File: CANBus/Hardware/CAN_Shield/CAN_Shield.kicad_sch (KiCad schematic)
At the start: 12 parts, among them J1 Power, J2 PWM, J3 Analog, J4 PWM, J5 Analog, J6 Communication, J7 Digital, J8 Screw_Terminal_01x02, U2 TCAN1051HGV

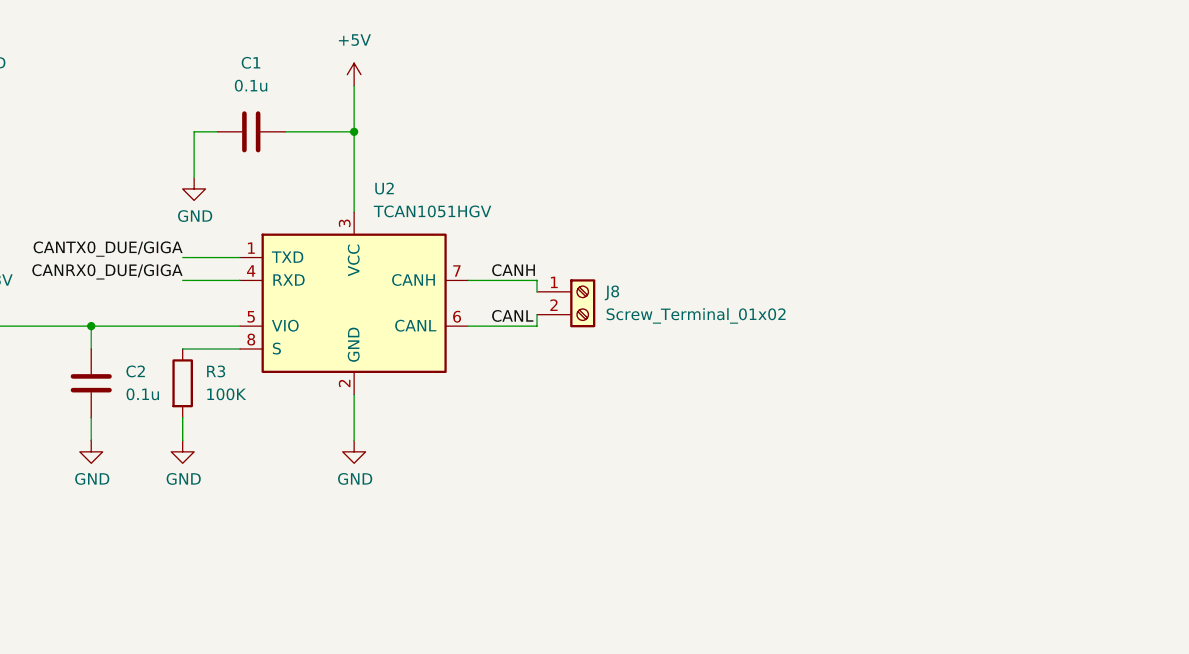
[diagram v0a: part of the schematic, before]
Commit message: feat: added  termination resistors and sent pin S to digital pin 2
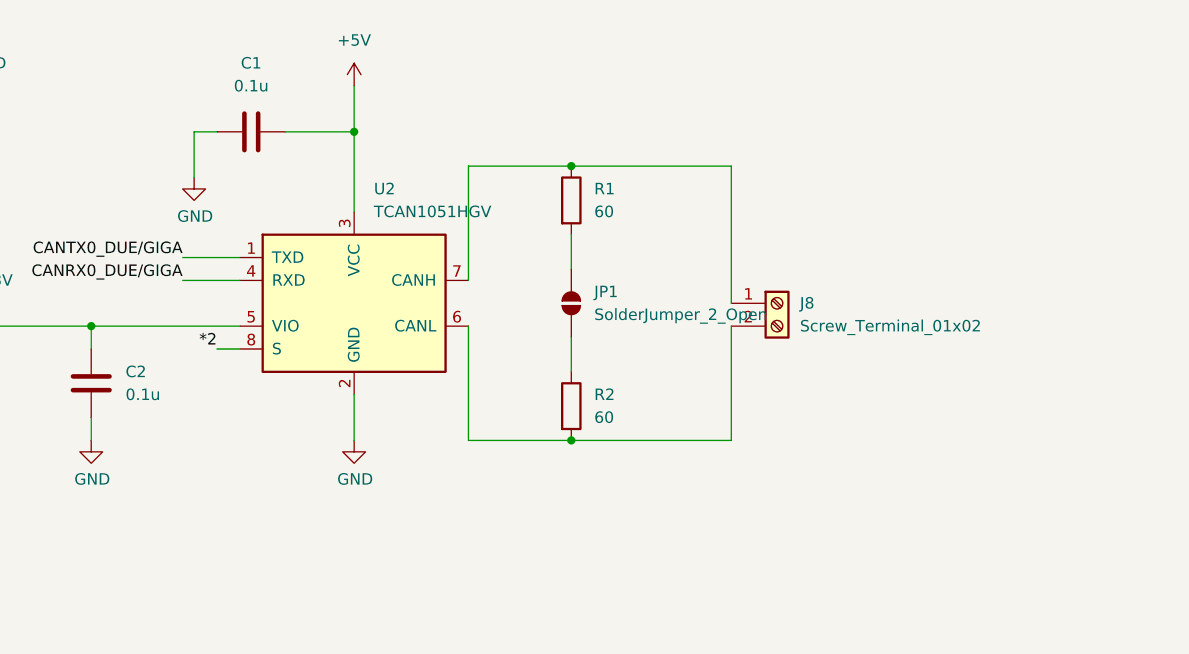
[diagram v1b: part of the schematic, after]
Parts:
- removed R3: 100K, symbol Device:R
- added JP1: SolderJumper_2_Open, symbol Jumper:SolderJumper_2_Open
- added R1, R2: 60, symbol Device:R
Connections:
- net *2: now also U2.8 (S)
- net CANH: no longer names the net of J8.1 (Pin_1), U2.7 (CANH)
- net CANH: now also R1.1
- net CANL: no longer names the net of J8.2 (Pin_2), U2.6 (CANL)
- net CANL: now also R2.2
- new net: JP1.1 (A), R2.1
- new net: JP1.2 (B), R1.2
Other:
- moved on the sheet: J8

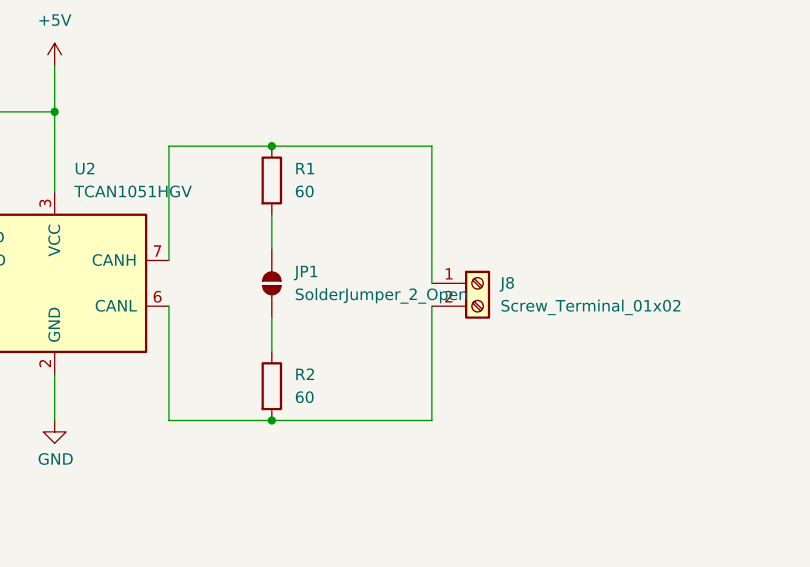
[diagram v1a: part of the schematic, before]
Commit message: fix: change to bridged solder jumper and remove backup files
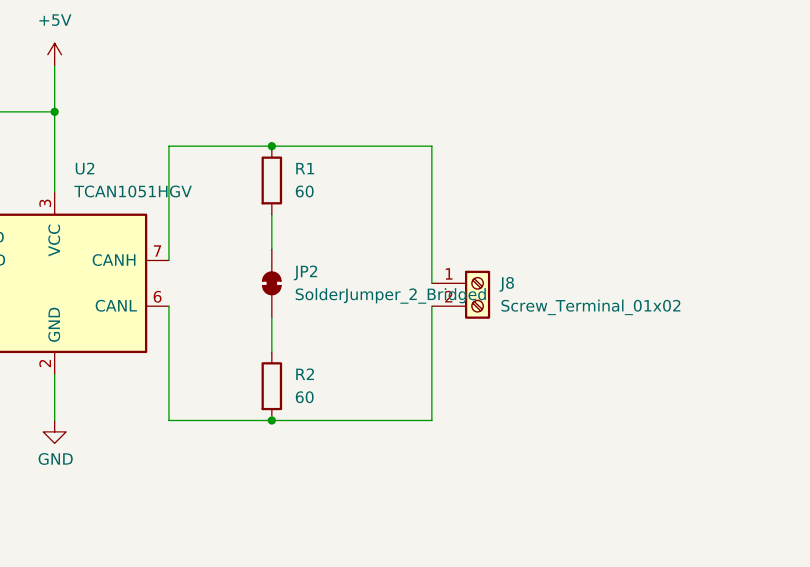
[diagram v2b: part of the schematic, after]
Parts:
- removed JP1: SolderJumper_2_Open, symbol Jumper:SolderJumper_2_Open
- added JP2: SolderJumper_2_Bridged, symbol Jumper:SolderJumper_2_Bridged
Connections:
- net at R2.1: now also JP2.1 (A)
- net at R1.2: now also JP2.2 (B)
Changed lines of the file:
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@@
 	(wire
 		(pts
-			(xy 146.05 71.12) (xy 146.05 74.93)
-		)
-		(stroke
-			(width 0)
-			(type default)
-		)
-	)
-	(wire
-		(pts
 			(xy 74.93 119.38) (xy 74.93 132.08)
 		)
@@
 	(wire
 		(pts
-			(xy 146.05 59.69) (xy 146.05 63.5)
-		)
-		(stroke
-			(width 0)
-			(type default)
-		)
-	)
-	(wire
-		(pts
 			(xy 20.32 46.99) (xy 20.32 49.53)
 		)
@@
 	(wire
 		(pts
+			(xy 146.05 71.12) (xy 146.05 74.93)
+		)
+		(stroke
+			(width 0)
+			(type default)
+		)
+	)
+	(wire
+		(pts
 			(xy 63.5 97.79) (xy 76.2 97.79)
 		)
@@
 	(wire
 		(pts
+			(xy 146.05 59.69) (xy 146.05 63.5)
+		)
+		(stroke
+			(width 0)
+			(type default)
+		)
+	)
+	(wire
+		(pts
 			(xy 39.37 132.08) (xy 39.37 142.24)
 		)
@@
 	)
 	(symbol
-		(lib_id "Jumper:SolderJumper_2_Open")
-		(at 146.05 67.31 90)
-		(unit 1)
-		(exclude_from_sim yes)
-		(in_bom no)
-		(on_board yes)
-		(dnp no)
-		(fields_autoplaced yes)
-		(property "Reference" "JP1"
-			(at 148.59 66.0399 90)
-			(effects
-				(font
-					(size 1.27 1.27)
-				)
-				(justify right)
-			)
-		)
-		(property "Value" "SolderJumper_2_Open"
-			(at 148.59 68.5799 90)
-			(effects
-				(font
-					(size 1.27 1.27)
-				)
-				(justify right)
-			)
-		)
-		(property "Footprint" ""
-			(at 146.05 67.31 0)
-			(effects
-				(font
-					(size 1.27 1.27)
-				)
-				(hide yes)
-			)
-		)
-		(property "Datasheet" "~"
-			(at 146.05 67.31 0)
-			(effects
-				(font
-					(size 1.27 1.27)
-				)
-				(hide yes)
-			)
-		)
-		(property "Description" "Solder Jumper, 2-pole, open"
-			(at 146.05 67.31 0)
-			(effects
-				(font
-					(size 1.27 1.27)
-				)
-				(hide yes)
-			)
-		)
-		(pin "1"
-		)
-		(pin "2"
-		)
-		(instances
-			(project "CAN_Shield"
-				(path "/e63e39d7-6ac0-4ffd-8aa3-1841a4541b55"
-					(reference "JP1")
-					(unit 1)
-				)
-			)
-		)
-	)
-	(symbol
 		(lib_id "power:VCC")
 		(at 26.67 26.67 0)
@@
 					(unit 1)
 				)
+			)
+		)
+	)
+	(symbol
+		(lib_id "Jumper:SolderJumper_2_Bridged")
+		(at 146.05 67.31 90)
+		(unit 1)
+		(exclude_from_sim yes)
+		(in_bom no)
+		(on_board yes)
+		(dnp no)
+		(fields_autoplaced yes)
+		(property "Reference" "JP2"
+			(at 148.59 66.0399 90)
+			(effects
+				(font
+					(size 1.27 1.27)
+				)
+				(justify right)
+			)
+		)
+		(property "Value" "SolderJumper_2_Bridged"
+			(at 148.59 68.5799 90)
+			(effects
+				(font
+					(size 1.27 1.27)
+				)
+				(justify right)
+			)
+		)
+		(property "Footprint" ""
+			(at 146.05 67.31 0)
+			(effects
+				(font
+					(size 1.27 1.27)
+				)
+				(hide yes)
+			)
+		)
+		(property "Datasheet" "~"
+			(at 146.05 67.31 0)
+			(effects
+				(font
+					(size 1.27 1.27)
+				)
+				(hide yes)
+			)
+		)
+		(property "Description" "Solder Jumper, 2-pole, closed/bridged"
+			(at 146.05 67.31 0)
+			(effects
+				(font
+					(size 1.27 1.27)
+				)
+				(hide yes)
+			)
+		)
+		(pin "2"
+		)
+		(pin "1"
+		)
+		(instances
+			(project "CAN_Shield"
+				(path "/e63e39d7-6ac0-4ffd-8aa3-1841a4541b55"
+					(reference "JP2")
+					(unit 1)
+				)

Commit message: feat: added PCB design
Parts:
- C1, C2: footprint (none) -> Capacitor_SMD:C_0805_2012Metric_Pad1.18x1.45mm_HandSolder; LCSC# (none) -> C38141; Proveedor (none) -> LCSC; manf# (none) -> 0805B104K500NT
- J1, J2, J3, J4, J5, J6: Proveedor (none) -> MOUSER/Digikey; manf# (none) -> PRT-14322
- J7: Proveedor (none) -> MOUSER; manf# (none) -> PRT-12790
- J8: footprint (none) -> TerminalBlock:TerminalBlock_bornier-2_P5.08mm; Proveedor (none) -> Steren; manf# (none) -> TRT-02
- JP2: footprint (none) -> Connector_PinHeader_2.54mm:PinHeader_1x02_P2.54mm_Vertical; LCSC# (none) -> C492401; Proveedor (none) -> LCSC; manf# (none) -> PZ254V-11-02P
- R1, R2: footprint (none) -> Resistor_SMD:R_0201_0603Metric; LCSC# (none) -> C166918; Proveedor (none) -> LCSC; manf# (none) -> RTT0360R0FTP
- U2: footprint (none) -> Package_SO:SOIC-8_3.9x4.9mm_P1.27mm; LCSC# (none) -> C424093; Proveedor (none) -> LCSC; manf# (none) -> MCP73831T-2ACI/OT
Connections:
- net +3.3V is gone; now on net +3V3: C2.1, U2.5 (VIO)

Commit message: feat: Resistors got changed
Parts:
- R1, R2: footprint Resistor_SMD:R_0201_0603Metric -> Resistor_SMD:R_1206_3216Metric_Pad1.30x1.75mm_HandSolder; LCSC# C166918 -> (none); Proveedor LCSC -> MOUSER; manf# RTT0360R0FTP -> 71-CRCW120660R0KNAIF
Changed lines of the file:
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@@
 			)
 		)
-		(property "Footprint" "Resistor_SMD:R_0201_0603Metric"
+		(property "Footprint" "Resistor_SMD:R_1206_3216Metric_Pad1.30x1.75mm_HandSolder"
 			(at 144.272 78.74 90)
 			(effects
@@
 			)
 		)
-		(property "LCSC#" " C166918"
-			(at 146.05 78.74 0)
-			(effects
-				(font
-					(size 1.27 1.27)
-				)
-				(hide yes)
-			)
-		)
-		(property "Proveedor" "LCSC"
-			(at 146.05 78.74 0)
-			(effects
-				(font
-					(size 1.27 1.27)
-				)
-				(hide yes)
-			)
-		)
-		(property "manf#" " RTT0360R0FTP"
+		(property "LCSC#" ""
+			(at 146.05 78.74 0)
+			(effects
+				(font
+					(size 1.27 1.27)
+				)
+				(hide yes)
+			)
+		)
+		(property "Proveedor" "MOUSER"
+			(at 146.05 78.74 0)
+			(effects
+				(font
+					(size 1.27 1.27)
+				)
+				(hide yes)
+			)
+		)
+		(property "manf#" "71-CRCW120660R0KNAIF"
 			(at 146.05 78.74 0)
 			(effects
@@
 			)
 		)
-		(property "Footprint" "Resistor_SMD:R_0201_0603Metric"
+		(property "Footprint" "Resistor_SMD:R_1206_3216Metric_Pad1.30x1.75mm_HandSolder"
 			(at 144.272 55.88 90)
 			(effects
@@
 			)
 		)
-		(property "LCSC#" " C166918"
-			(at 146.05 55.88 0)
-			(effects
-				(font
-					(size 1.27 1.27)
-				)
-				(hide yes)
-			)
-		)
-		(property "Proveedor" "LCSC"
-			(at 146.05 55.88 0)
-			(effects
-				(font
-					(size 1.27 1.27)
-				)
-				(hide yes)
-			)
-		)
-		(property "manf#" " RTT0360R0FTP"
-			(at 146.05 55.88 0)
-			(effects
+		(property "LCSC#" ""
+			(at 146.05 55.88 0)
+			(effects
+				(font
+					(size 1.27 1.27)
+				)
+				(hide yes)
+			)
+		)
+		(property "Proveedor" "MOUSER"
+			(at 146.05 55.88 0)
+			(effects
+				(font
+					(size 1.27 1.27)
+				)
+				(hide yes)
+			)
+		)
+		(property "manf#" "71-CRCW120660R0KNAIF"
+			(at 146.05 55.88 0)
+			(effects

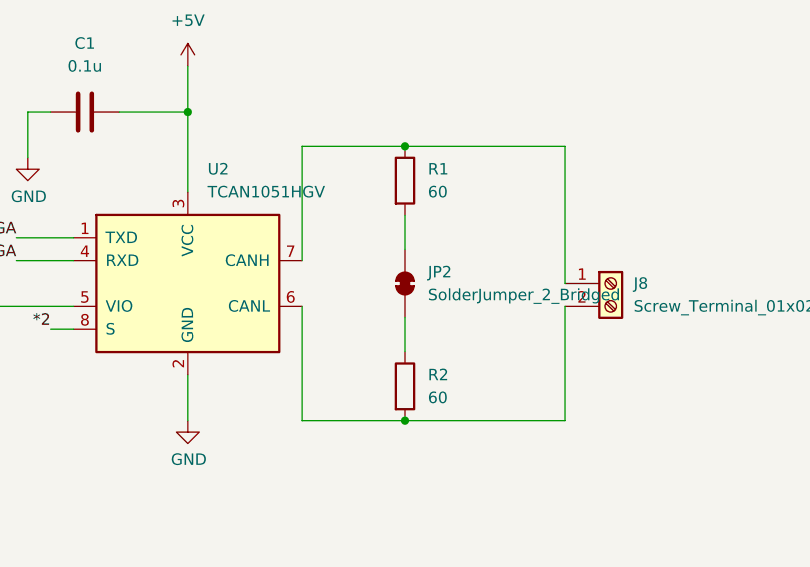
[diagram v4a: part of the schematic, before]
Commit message: feat(Hw): Route PCB
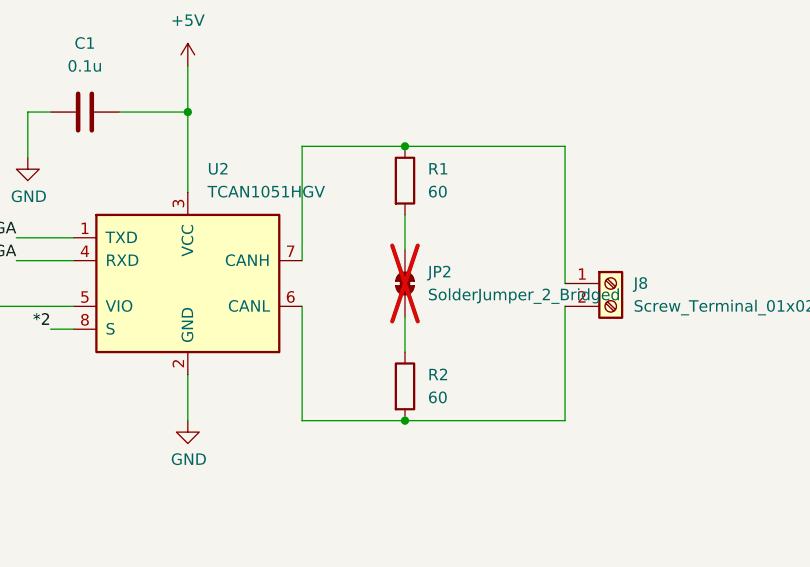
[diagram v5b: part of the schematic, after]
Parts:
- JP2: footprint Connector_PinHeader_2.54mm:PinHeader_1x02_P2.54mm_Vertical -> Jumper:SolderJumper-2_P1.3mm_Bridged_Pad1.0x1.5mm; LCSC# C492401 -> (none); Proveedor LCSC -> (none); manf# PZ254V-11-02P -> (none); now not fitted
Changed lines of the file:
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@@
 		(in_bom no)
 		(on_board yes)
-		(dnp no)
+		(dnp yes)
 		(fields_autoplaced yes)
 		(property "Reference" "JP2"
@@
 			)
 		)
-		(property "Footprint" "Connector_PinHeader_2.54mm:PinHeader_1x02_P2.54mm_Vertical"
+		(property "Footprint" "Jumper:SolderJumper-2_P1.3mm_Bridged_Pad1.0x1.5mm"
 			(at 146.05 67.31 0)
 			(effects
@@
 			)
 		)
-		(property "LCSC#" "C492401"
+		(property "LCSC#" ""
 			(at 146.05 67.31 0)
 			(effects
@@
 			)
 		)
-		(property "Proveedor" "LCSC"
+		(property "Proveedor" ""
 			(at 146.05 67.31 0)
 			(effects
@@
 			)
 		)
-		(property "manf#" "PZ254V-11-02P "
+		(property "manf#" ""
 			(at 146.05 67.31 0)
 			(effects

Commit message: feat(hw): Bom updated
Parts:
- U2: LCSC# C424093 -> (none); Proveedor LCSC -> MOUSER; manf# MCP73831T-2ACI/OT -> 595-TCAN1051HGVDR
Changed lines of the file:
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@@
 			)
 		)
-		(property "LCSC#" " C424093"
+		(property "LCSC#" ""
 			(at 121.92 67.31 0)
 			(effects
@@
 			)
 		)
-		(property "Proveedor" "LCSC"
+		(property "Proveedor" "MOUSER"
 			(at 121.92 67.31 0)
 			(effects
@@
 			)
 		)
-		(property "manf#" " MCP73831T-2ACI/OT"
+		(property "manf#" "595-TCAN1051HGVDR"
 			(at 121.92 67.31 0)
 			(effects
